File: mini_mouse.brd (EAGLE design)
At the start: 92 x 92 mm, 32 parts, among them IC1 PIC18F4550_TQFP, IC3 LP2950CDT-5.0, IC4 L293D

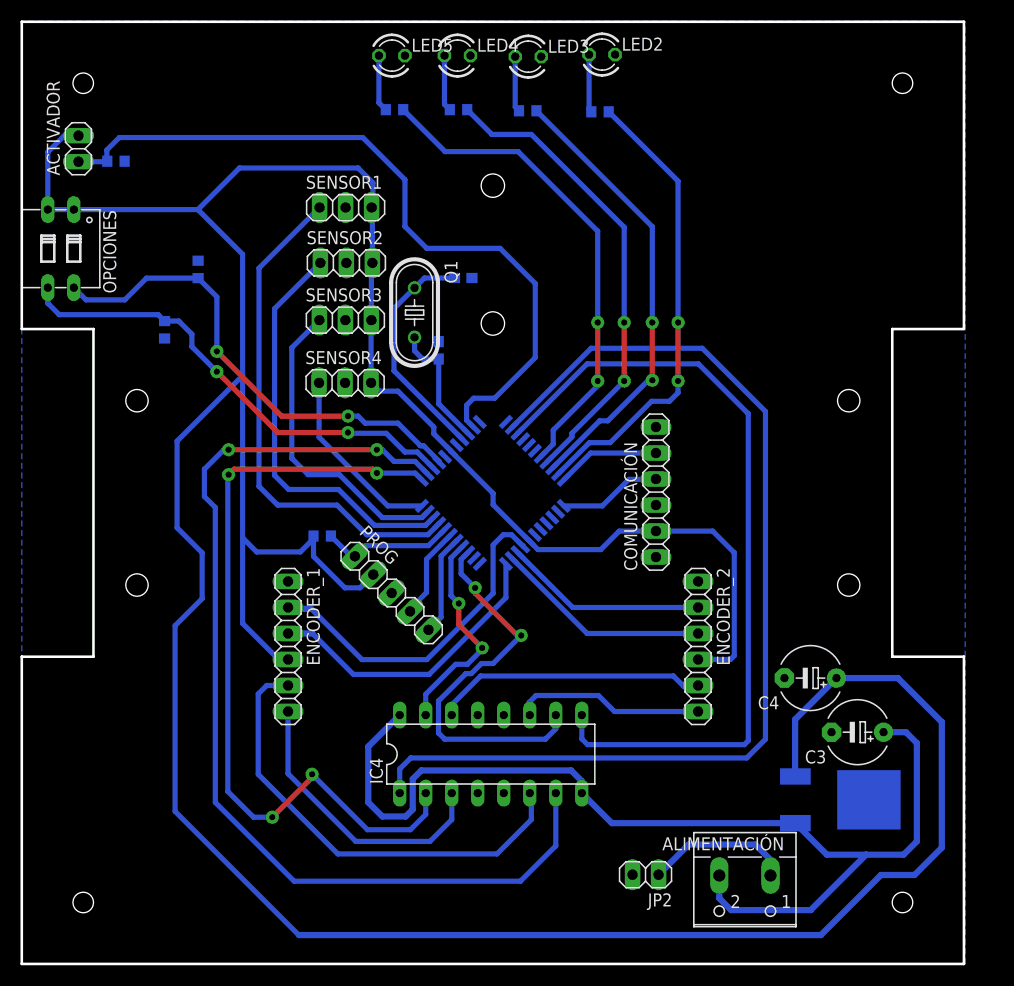
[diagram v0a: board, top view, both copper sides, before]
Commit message: Acomodo de pines comunicación y puentes
Se acomodaron los puentes y se cambió el conector para el módulo Bluetooth
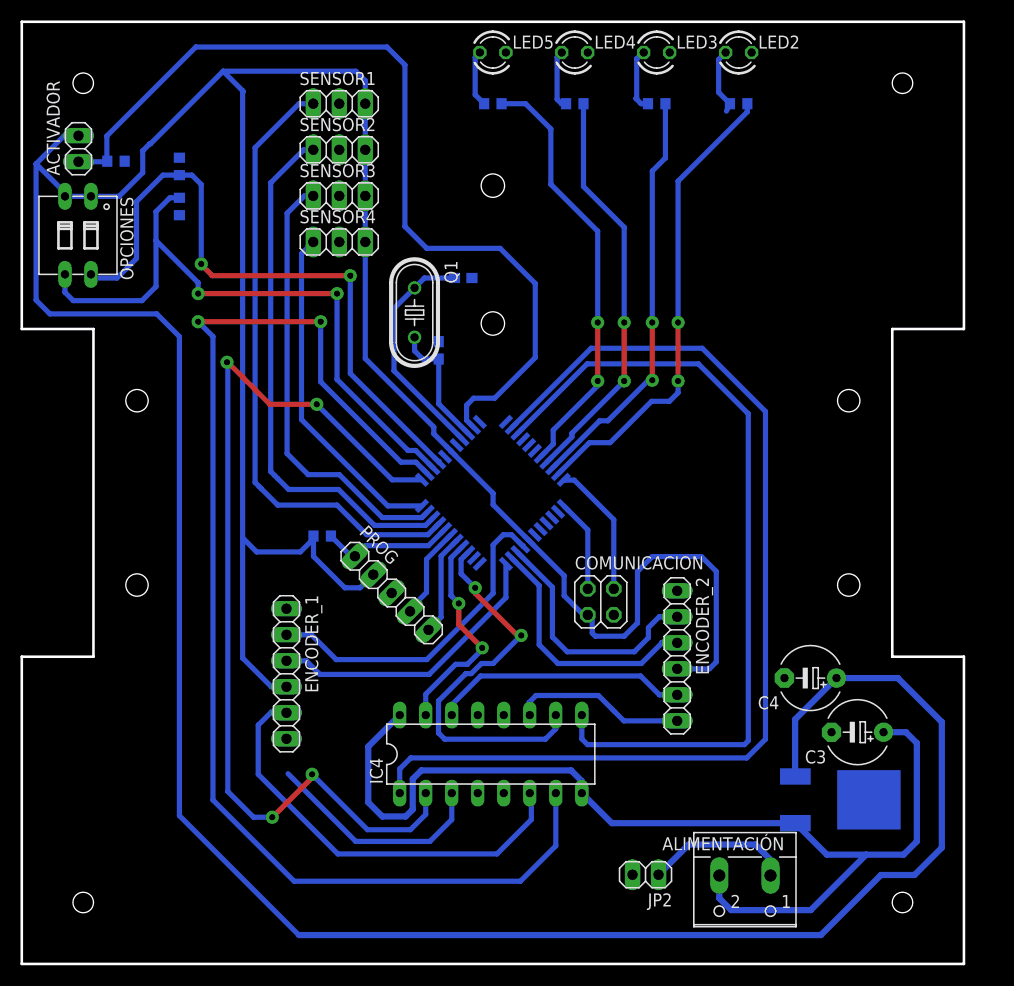
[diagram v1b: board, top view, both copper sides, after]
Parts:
- removed COMUNICACIÓN: (no value), pinhead:1X06
- added COMUNICACION: (no value), pinhead:2X02
- moved SENSOR4 13.8 mm to (31.0, 70.5)
- moved R_L1 13.6 mm to (70.0, 84.0)
- moved LED2 13.3 mm to (70.0, 89.0)
- moved R_L2 12.6 mm to (62.0, 84.0)
- moved LED3 12.6 mm to (62.0, 89.0)
- moved SENSOR3 12.1 mm to (31.0, 75.0)
- moved RS1 12.1 mm to (15.4, 74.0)
- moved LED4 11.5 mm to (54.0, 89.0)
- moved R_L3 11.4 mm to (54.0, 84.0)
- moved SENSOR2 11.1 mm to (31.0, 79.5)
- moved RS2 10.2 mm to (15.4, 77.9)
- moved SENSOR1 10.2 mm to (31.0, 84.0)
- moved LED5 9.86 mm to (46.0, 89.0)
- moved R_L4 9.62 mm to (46.0, 84.0)
- moved ENCODER_1 2.67 mm to (25.8, 28.3)
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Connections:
- net +5V: now also COMUNICACION.1; no longer COMUNICACIÓN.2
- net GND: now also COMUNICACION.3; no longer COMUNICACIÓN.3
- net RX: now also COMUNICACION.2; no longer COMUNICACIÓN.4
- net TX: now also COMUNICACION.4; no longer COMUNICACIÓN.5
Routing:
- net +5V: track 355.1 -> 417.7 mm
- net D2_M1: track 99.6 -> 122.7 mm
- net PA_1: track 46.6 -> 63.6 mm
- net PA_2: track 47.7 -> 63.5 mm
- net D1_M1: track 77.7 -> 92.9 mm
- net S4: track 18.1 -> 33.1 mm
- net START: track 73.2 -> 87.9 mm
- net S3: track 30.5 -> 43.3 mm
- net S2: track 40.5 -> 52.1 mm
- net S1: track 49.7 -> 60.7 mm
- net LED_3: track 46.2 -> 39.8 mm
- net LED_4: track 48.2 -> 42.0 mm
- net M1_1: track 28.3 -> 22.2 mm
- net OUT_A2: track 19.9 -> 24.5 mm
- net OUT_B2: track 21.3 -> 24.7 mm
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- removed copper zone on layer 16, net GND

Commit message: Cambios en puentes
Se hicieron modificaciones en los puentes para una mejor limpieza en la placa
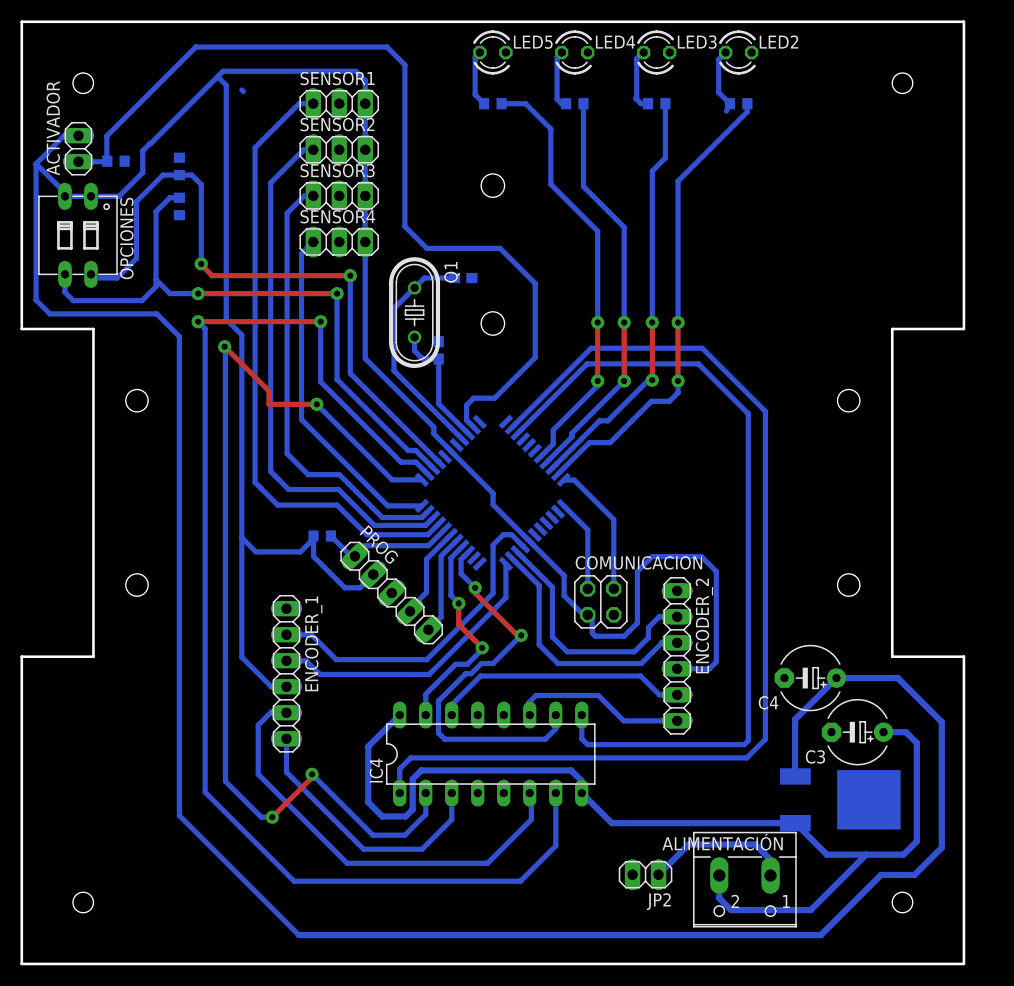
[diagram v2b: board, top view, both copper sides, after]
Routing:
- net M1_1: track 22.2 -> 26.3 mm
- net D1_M1: track 92.9 -> 96.2 mm
- net PA_1: track 63.6 -> 61.3 mm
- net M2_1: track 42.1 -> 42.8 mm

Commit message: Leds re-acomodados
Se  acomodaron los LEDS del lado derecho de la placa.
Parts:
- removed PROG: (no value), pinhead:1X05
- added JP1: (no value), pinhead:2X03
- moved LED5 42.8 mm to (88.0, 81.0)
- moved LED4 36.2 mm to (88.0, 76.5)
- moved R_L4 35.0 mm to (81.0, 83.0)
- moved LED3 31.1 mm to (88.0, 72.0)
- moved LED2 28.0 mm to (88.0, 67.5)
- moved R_L3 27.9 mm to (81.0, 77.0)
- moved R_L2 22.7 mm to (81.0, 71.5)
- moved R_L1 21.5 mm to (81.0, 65.5)
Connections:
- net +5V: now also JP1.2; no longer PROG.2
- net GND: now also JP1.1, JP1.3; no longer PROG.3
- net LED_1: no longer IC1.2
- net LED_2: no longer IC1.3
- net LED_3: no longer IC1.4
- net LED_4: no longer IC1.5
- net MCLR: now also JP1.4; no longer PROG.1
- net PGC: now also JP1.5; no longer PROG.5
- net PGD: now also JP1.6; no longer PROG.4
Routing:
- net LED_4: track 42.0 -> 55.7 mm
- net LED_3: track 39.8 -> 50.3 mm
- net N$1: track 6.54 -> 0.00 mm
- net N$2: track 6.24 -> 0.00 mm
- net N$3: track 5.81 -> 0.00 mm
- net MCLR: track 13.1 -> 18.7 mm
- net N$4: track 5.55 -> 0.00 mm
- net LED_2: track 40.9 -> 45.9 mm
- net LED_1: track 46.0 -> 41.7 mm
- net PGC: track 9.85 -> 12.6 mm
- net START: track 87.9 -> 85.3 mm
- net OUT_A1: track 32.5 -> 34.1 mm
- net OUT_B1: track 28.4 -> 29.6 mm
- net PGD: track 9.13 -> 9.95 mm
- net +5V: track 417.5 -> 417.0 mm
